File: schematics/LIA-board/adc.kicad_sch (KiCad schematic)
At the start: 1 part, among them U14 ADS1220xPW

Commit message: all current changes
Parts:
- added U15: DAC80508, Package_SON:Texas_DRX_WSON-10_2.5x2.5mm_P0.5mm, symbol CERN:DAC80508ZRTE
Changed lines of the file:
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@@
+		)
+	)
+	(symbol
+		(lib_id "CERN:DAC80508ZRTE")
+		(at 137.16 119.38 0)
+		(unit 1)
+		(body_style 1)
+		(exclude_from_sim no)
+		(in_bom yes)
+		(on_board yes)
+		(in_pos_files yes)
+		(dnp no)
+		(fields_autoplaced yes)
+		(property "Reference" "U15"
+			(at 149.86 114.3 0)
+			(show_name no)
+			(do_not_autoplace no)
+			(effects
+				(font
+					(size 1.524 1.524)
+				)
+			)
+		)
+		(property "Value" "DAC80508"
+			(at 149.86 116.84 0)
+			(show_name no)
+			(do_not_autoplace no)
+			(effects
+				(font
+					(size 1.524 1.524)
+				)
+			)
+		)
+		(property "Footprint" "Package_SON:Texas_DRX_WSON-10_2.5x2.5mm_P0.5mm"
+			(at 137.16 119.38 0)
+			(hide yes)
+			(show_name no)
+			(do_not_autoplace no)
+			(effects
+				(font
+					(size 1.27 1.27)
+				)
+			)
+		)
+		(property "Datasheet" ""
+			(at 137.16 119.38 0)
+			(hide yes)
+			(show_name no)
+			(do_not_autoplace no)
+			(effects
+				(font
+					(size 1.27 1.27)
+				)
+			)
+		)
+		(property "Description" "Octal, 16-Bit, SPI, Voltage Output DAC With Internal Reference"
+			(at 137.16 119.38 0)
+			(hide yes)
+			(show_name no)
+			(do_not_autoplace no)
+			(effects
+				(font
+					(size 1.27 1.27)
+				)
+			)
+		)
+		(pin "9"
+		)
+		(pin "10"
+		)
+		(pin "11"
+		)
+		(pin "12"
+		)
+		(pin "13"
+		)
+		(pin "14"
+		)
+		(pin "15"
+		)
+		(pin "16"
+		)
+		(pin "1"
+		)
+		(pin "4"
+		)
+		(pin "5"
+		)
+		(pin "3"
+		)
+		(pin "2"
+		)
+		(pin "17"
+		)
+		(pin "6"
+		)
+		(pin "7"
+		)
+		(pin "8"
+		)
+		(instances
+			(project "GMOS-LIA"
+				(path "/87b3d1ed-39bd-4cff-a405-e580c48ff0ef/c2b448c7-1606-40e4-b2d6-d927d0381aee"
+					(reference "U15")
+					(unit 1)
+				)
+			)
 		)
 	)

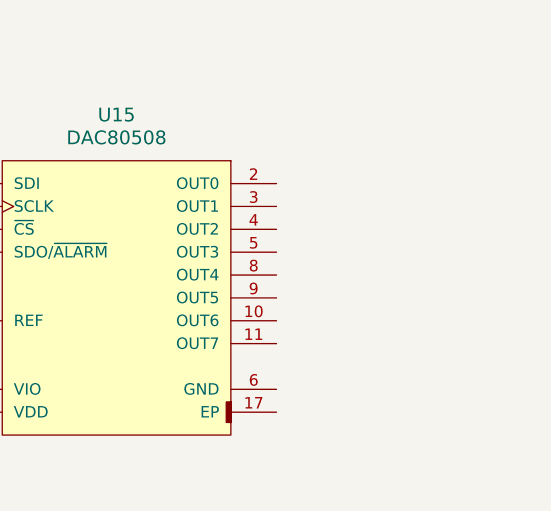
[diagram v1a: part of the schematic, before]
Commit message: added MCU
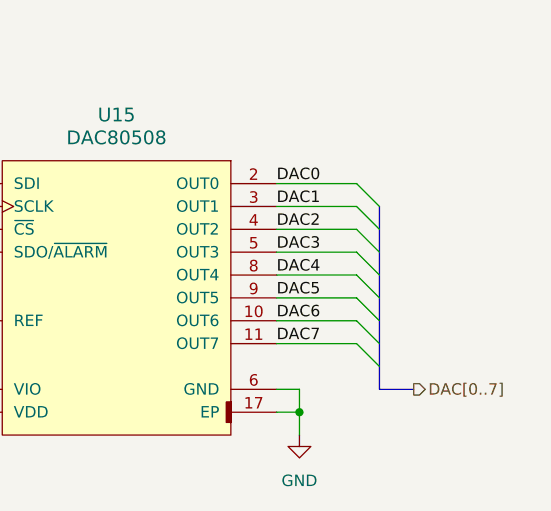
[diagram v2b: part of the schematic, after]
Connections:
- net DAC6: now reaches U15.10 (OUT6)
- net DAC7: now reaches U15.11 (OUT7)
- net GND: now reaches U15.17 (EP)
- net GND: now also U15.6 (GND)
- net DAC0: now reaches U15.2 (OUT0)
- net DAC1: now reaches U15.3 (OUT1)
- net DAC2: now reaches U15.4 (OUT2)
- net DAC3: now reaches U15.5 (OUT3)
- net DAC4: now reaches U15.8 (OUT4)
- net DAC5: now reaches U15.9 (OUT5)

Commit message: modified scematic
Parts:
- removed U15: DAC80508, Package_SON:Texas_DRX_WSON-10_2.5x2.5mm_P0.5mm, symbol CERN:DAC80508ZRTE

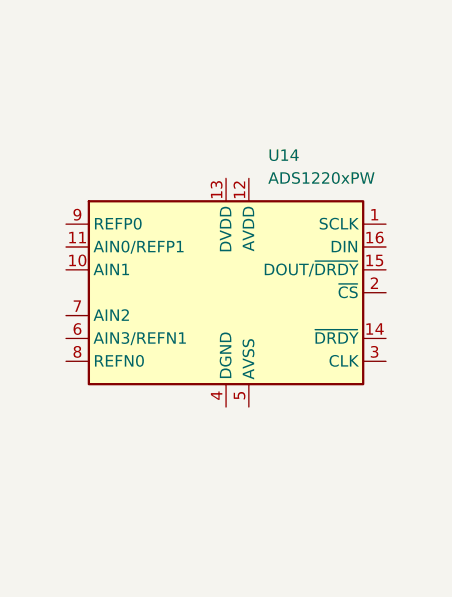
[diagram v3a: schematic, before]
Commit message: commit before changing the oscillator implementation
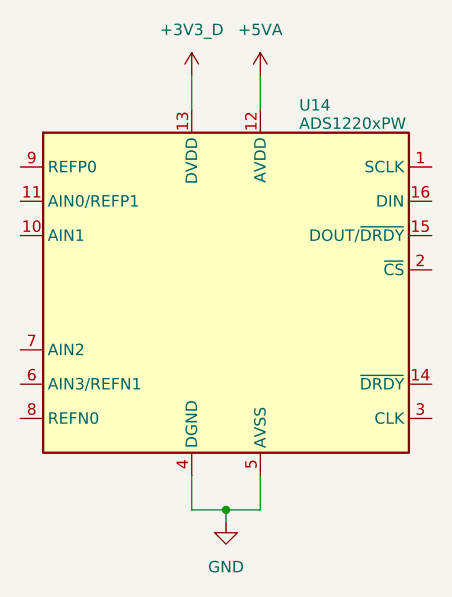
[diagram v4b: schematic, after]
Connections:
- net +5VA: now reaches U14.12 (AVDD)
- net +3V3_D: now reaches U14.13 (DVDD)
- net GND: now reaches U14.4 (DGND)
- net GND: now also U14.5 (AVSS)

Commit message: commit before changing LIA
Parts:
- renumbered U14 to U7
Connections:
- net spi_clk: now reaches U7.1 (SCLK)
- net spi_miso: now reaches U7.15 (DOUT/~{DRDY})
- net spi_mosi: now reaches U7.16 (DIN)
- net adc_cs: now reaches U7.2 (~{CS})
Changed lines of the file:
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@@
+	(wire
+		(pts
+			(xy 172.72 81.28) (xy 184.15 81.28)
+		)
+		(stroke
+			(width 0)
+			(type default)
+		)
+	)
 	(wire
 		(pts
@@
 	(wire
 		(pts
+			(xy 172.72 77.47) (xy 184.15 77.47)
+		)
+		(stroke
+			(width 0)
+			(type default)
+		)
+	)
+	(wire
+		(pts
 			(xy 146.05 63.5) (xy 146.05 67.31)
 		)
@@
 	(wire
 		(pts
+			(xy 172.72 73.66) (xy 184.15 73.66)
+		)
+		(stroke
+			(width 0)
+			(type default)
+		)
+	)
+	(wire
+		(pts
+			(xy 111.76 77.47) (xy 127 77.47)
+		)
+		(stroke
+			(width 0)
+			(type default)
+		)
+	)
+	(wire
+		(pts
+			(xy 111.76 81.28) (xy 127 81.28)
+		)
+		(stroke
+			(width 0)
+			(type default)
+		)
+	)
+	(wire
+		(pts
+			(xy 172.72 85.09) (xy 184.15 85.09)
+		)
+		(stroke
+			(width 0)
+			(type default)
+		)
+	)
+	(wire
+		(pts
 			(xy 146.05 111.76) (xy 153.67 111.76)
 		)
@@
 			(width 0)
 			(type default)
+		)
+	)
+	(hierarchical_label "spi_miso"
+		(shape output)
+		(at 184.15 81.28 0)
+		(effects
+			(font
+				(size 1.27 1.27)
+			)
+			(justify left)
+		)
+	)
+	(hierarchical_label "spi_mosi"
+		(shape input)
+		(at 184.15 77.47 0)
+		(effects
+			(font
+				(size 1.27 1.27)
+			)
+			(justify left)
+		)
+	)
+	(hierarchical_label "spi_clk"
+		(shape input)
+		(at 184.15 73.66 0)
+		(effects
+			(font
+				(size 1.27 1.27)
+			)
+			(justify left)
+		)
+	)
+	(hierarchical_label "adc_cs"
+		(shape input)
+		(at 184.15 85.09 0)
+		(effects
+			(font
+				(size 1.27 1.27)
+			)
+			(justify left)
 		)
 	)
@@
 		(dnp no)
 		(fields_autoplaced yes)
-		(property "Reference" "#PWR0104"
+		(property "Reference" "#PWR037"
 			(at 153.67 67.31 0)
 			(hide yes)
@@
 			(project "GMOS-LIA"
 				(path "/87b3d1ed-39bd-4cff-a405-e580c48ff0ef/c2b448c7-1606-40e4-b2d6-d927d0381aee"
-					(reference "#PWR0104")
+					(reference "#PWR037")
 					(unit 1)
 				)
@@
 		(dnp no)
 		(fields_autoplaced yes)
-		(property "Reference" "U14"
+		(property "Reference" "U7"
 			(at 157.988 66.802 0)
 			(show_name no)
@@
 			(project "GMOS-LIA"
 				(path "/87b3d1ed-39bd-4cff-a405-e580c48ff0ef/c2b448c7-1606-40e4-b2d6-d927d0381aee"
-					(reference "U14")
+					(reference "U7")
 					(unit 1)
 				)
@@
 		(dnp no)
 		(fields_autoplaced yes)
-		(property "Reference" "#PWR0102"
+		(property "Reference" "#PWR038"
 			(at 149.86 119.38 0)
 			(hide yes)
@@
 			(project "GMOS-LIA"
 				(path "/87b3d1ed-39bd-4cff-a405-e580c48ff0ef/c2b448c7-1606-40e4-b2d6-d927d0381aee"
-					(reference "#PWR0102")
+					(reference "#PWR038")
 					(unit 1)
 				)
@@
 		(dnp no)
 		(fields_autoplaced yes)
-		(property "Reference" "#PWR0103"
+		(property "Reference" "#PWR036"
 			(at 146.05 67.31 0)
 			(hide yes)
@@
 			(project "GMOS-LIA"
 				(path "/87b3d1ed-39bd-4cff-a405-e580c48ff0ef/c2b448c7-1606-40e4-b2d6-d927d0381aee"
-					(reference "#PWR0103")
+					(reference "#PWR036")
 					(unit 1)
 				)
